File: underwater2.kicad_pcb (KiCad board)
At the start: 2 copper layers, 99.1 x 99.1 mm, 79 parts, among them IC1 ICM-20948, J1 Motor1, J10 ICM20948 out, J11 Pow, J12 serial, J13 serial2, J14 5v pow, J15 5v pow, J2 Motor2, J3 Raspberry_Pi_2_3, J4 USB_C_Receptacle_USB2.0, J5 USB out, J6 Water, J7 Power, J8 Light, J9 MotorPow, SW1 SW_Push, SW2 SW_Push, U1 FT230XS, U2 TB6612FNG, U3 TB6612FNG, U4 ESP32-WROOM-32, U5 LM1117-1.8, U7 LM1117-3.3

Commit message: Modify milestone 2020724
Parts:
- removed PS1: ACT4060ASH-T, SamacSys_Parts:SOIC127P605X175-8N
- removed U7: LM1117-3.3, Package_TO_SOT_SMD:SOT-223
- added C20: 10μF, Capacitor_SMD:C_1206_3216Metric, F.Cu at (168.1, 120.3)
- added IC2: KST10MTF, SOT95P240X120-3N, F.Cu at (155.6, 75.8)
- added IC3: ACT4070BYH-T, SOIC127P600X170-9N, F.Cu at (115.8, 55.6)
- added IC4: ICM-20948, SamacSys_Parts:QFN40P300X300X105-25N-D, F.Cu at (153.7, 63.5)
- added J16: MotorPow, Connector_PinHeader_2.54mm:PinHeader_1x02_P2.54mm_Vertical, F.Cu at (173.2, 120.7)
- added SW3: SW_DIP_x01, Button_Switch_THT:SW_E-Switch_EG1271_DPDT, F.Cu at (123.8, 129.6)
- added U6: TB6612FNG, Package_SO:SSOP-24_5.3x8.2mm_P0.65mm, F.Cu at (161.0, 120.5)
- C1: value 10μF -> 10nF/25V; footprint Capacitor_SMD:C_1206_3216Metric -> Capacitor_SMD:C_0603_1608Metric
- C10: value 10μF -> 1nF/16V; footprint Capacitor_SMD:C_1206_3216Metric -> Capacitor_SMD:C_0603_1608Metric
- C11: value 10nF50V -> 22µF/10V; footprint Capacitor_SMD:C_1206_3216Metric -> Capacitor_SMD:C_0603_1608Metric
- C12, C13: value 0.1μF -> 0μF
- C14: value 22μF10V -> 0.1μF
- C15: value 0.1μF -> 10μF
- C16: value 2.2nF6.3V -> 0.1μF
- C17: value 10μF35V -> 0.1μF
- C18, C19: value 0μF -> 0.1μF
- C2: value 47pF -> 10µF/50V
- C3: value 47pF -> 10nF
- C5: value 0.1μF -> 4.7μF
- C6: value 0.1μF -> 100nF
- C7: value 4.7μF -> 4.7nF/25V; footprint Capacitor_SMD:C_1206_3216Metric -> Capacitor_SMD:C_0603_1608Metric
- C8: value 100nF -> if necessary
- C9: value 10μF -> ifnecessary
- D1: value RX -> 34/40V 3A; footprint Capacitor_SMD:C_1206_3216Metric -> SamacSys_Parts:DIONM7959X282N
- D2: value TX -> 34/40V 3A; footprint Capacitor_SMD:C_1206_3216Metric -> SamacSys_Parts:DIONM7959X282N
- D3: value Power -> TX
- D4: value DIODE -> RX; footprint SamacSys_Parts:DIONM7959X282N -> Capacitor_SMD:C_1206_3216Metric
- D5: value 34/40V 3A -> 40V/3A
- D6: value Power 3.3 -> POWER
- D7: value 34/40V 3A -> Power 3.3; footprint SamacSys_Parts:DIONM7959X282N -> Capacitor_SMD:C_1206_3216Metric
- D8: value 34/40V 3A -> DIODE
- FB1: value FB -> Ferrite_Bead_Small
- IC1: value ICM-20948 -> KST10MTF; footprint SamacSys_Parts:QFN40P300X300X105-25N-D -> SOT95P240X120-3N
- J1: value Motor1 -> 5v pow; footprint Connector_PinSocket_2.54mm:PinSocket_1x04_P2.54mm_Horizontal -> Connector_PinHeader_2.54mm:PinHeader_1x02_P2.54mm_Vertical
- J10: value ICM20948 out -> Power; footprint Connector_PinHeader_2.54mm:PinHeader_1x08_P2.54mm_Vertical -> Connector_PinHeader_2.54mm:PinHeader_1x02_P2.54mm_Horizontal
- J11: value Pow -> Light; footprint Connector_PinHeader_2.54mm:PinHeader_1x02_P2.54mm_Vertical -> Connector_PinHeader_2.54mm:PinHeader_1x03_P2.54mm_Vertical
- J12: value serial -> ICM20948 out; footprint Connector_PinHeader_2.54mm:PinHeader_1x02_P2.54mm_Vertical -> Connector_PinHeader_2.54mm:PinHeader_1x08_P2.54mm_Vertical
- J14: value 5v pow -> Motor1; footprint Connector_PinHeader_2.54mm:PinHeader_1x02_P2.54mm_Vertical -> Connector_PinSocket_2.54mm:PinSocket_1x04_P2.54mm_Horizontal
- J15: value 5v pow -> Motor2; footprint Connector_PinHeader_2.54mm:PinHeader_1x02_P2.54mm_Vertical -> Connector_PinSocket_2.54mm:PinSocket_1x04_P2.54mm_Horizontal
- J2: value Motor2 -> 5v pow; footprint Connector_PinSocket_2.54mm:PinSocket_1x04_P2.54mm_Horizontal -> Connector_PinHeader_2.54mm:PinHeader_1x02_P2.54mm_Vertical
- J3: value Raspberry_Pi_2_3 -> external regurator; footprint Connector_PinSocket_2.54mm:PinSocket_2x20_P2.54mm_Vertical -> Connector_PinSocket_2.54mm:PinSocket_1x03_P2.54mm_Vertical
- J5: value USB out -> Pow; footprint Connector_PinHeader_2.54mm:PinHeader_1x05_P2.54mm_Vertical -> Connector_PinHeader_2.54mm:PinHeader_1x02_P2.54mm_Vertical
- J6: value Water -> Raspberry_Pi_2_3; footprint Connector_PinHeader_2.54mm:PinHeader_1x02_P2.54mm_Horizontal -> Connector_PinSocket_2.54mm:PinSocket_2x20_P2.54mm_Vertical; moved to B.Cu
- J7: value Power -> serial; footprint Connector_PinHeader_2.54mm:PinHeader_1x02_P2.54mm_Horizontal -> Connector_PinHeader_2.54mm:PinHeader_1x02_P2.54mm_Vertical
- J8: value Light -> Conn_01x10_Female; footprint Connector_PinHeader_2.54mm:PinHeader_1x03_P2.54mm_Horizontal -> Connector_PinSocket_2.54mm:PinSocket_1x09_P2.54mm_Vertical
- J9: value MotorPow -> Water; footprint Connector_PinHeader_2.54mm:PinHeader_1x02_P2.54mm_Vertical -> Connector_PinHeader_2.54mm:PinHeader_1x02_P2.54mm_Horizontal
- JP1: value High Full -> Jumper_NC_Small; footprint Jumper:SolderJumper-3_P1.3mm_Open_RoundedPad1.0x1.5mm -> Jumper:SolderJumper-2_P1.3mm_Open_RoundedPad1.0x1.5mm
- JP2: value TX -> J usbpower; footprint Jumper:SolderJumper-2_P1.3mm_Open_Pad1.0x1.5mm -> Jumper:SolderJumper-2_P1.3mm_Open_RoundedPad1.0x1.5mm
- JP3: value RX -> J battpower; footprint Jumper:SolderJumper-2_P1.3mm_Open_Pad1.0x1.5mm -> Jumper:SolderJumper-2_P1.3mm_Open_RoundedPad1.0x1.5mm
- JP4: value J usbpower -> tx rx
- JP5: value J battpower -> rx tx
- L1: value 15μH -> 15µH4A; footprint Capacitor_SMD:C_1206_3216Metric -> SamacSys_Parts:B952ASH100MP3
- R1, R2: value 5.1k -> 10k
- R10: value 10k -> 270
- R11: value 1M -> 51k; footprint Capacitor_SMD:C_1206_3216Metric -> Capacitor_SMD:C_0603_1608Metric
- R12: value 330k -> 9.76k; footprint Capacitor_SMD:C_1206_3216Metric -> Capacitor_SMD:C_0603_1608Metric
- R13: value 28.7k -> 330k
- R14: value 15k -> 12k; footprint Capacitor_SMD:C_1206_3216Metric -> Capacitor_SMD:C_0603_1608Metric
- R15: value 1.5k High -> 270
- R16: value 1.5k Full -> 270
- R3: value 27 -> 10k
- R4: value 27 -> 5.1k
- R5: value 270 -> 5.1k
- R6, R7: value 270 -> 27
- R8: value 10k -> 1M
- SW1, SW2: value SW_Push -> SW_Push_Dual
- U1: value FT230XS -> FT232RL; footprint Package_SO:SSOP-16_3.9x4.9mm_P0.635mm -> Package_SO:SSOP-28_5.3x10.2mm_P0.65mm
- U2: value TB6612FNG -> LM1117-3.3; footprint Package_SO:SSOP-24_5.3x8.2mm_P0.65mm -> Package_TO_SOT_SMD:SOT-223
- U4: value ESP32-WROOM-32 -> LM1117-1.8; footprint RF_Module:ESP32-WROOM-32 -> Package_TO_SOT_SMD:SOT-223
- U5: value LM1117-1.8 -> ESP32-WROOM-32; footprint Package_TO_SOT_SMD:SOT-223 -> RF_Module:ESP32-WROOM-32
- moved R1 91.4 mm to (161.7, 75.9), turned to 180 degrees
- moved J14 90.1 mm to (142.5, 129.0)
- moved J15 88.3 mm to (158.9, 129.2), turned to 90 degrees
- moved J1 86.5 mm to (120.7, 43.9)
- moved R16 85.9 mm to (147.3, 64.4)
- moved J2 85.6 mm to (143.5, 43.8)
- moved C7 84.8 mm to (122.7, 54.1), turned to 0 degrees
- moved JP1 83.5 mm to (159.4, 79.9), turned to 180 degrees
- moved C1 83.0 mm to (110.9, 53.0), turned to 90 degrees
- moved J12 82.8 mm to (169.9, 58.9), turned to 0 degrees
- moved D8 82.5 mm to (170.4, 113.0), turned to 180 degrees
- moved R2 79.9 mm to (151.3, 77.7), turned to 270 degrees
- moved C2 79.7 mm to (108.2, 56.3)
- moved J13 74.6 mm to (103.3, 43.9), turned to 270 degrees
- moved SW2 73.2 mm to (159.0, 53.0), turned to 180 degrees
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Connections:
- C1 pad 2: GND -> Net-(C1-Pad2)
- C10 pad 1: -BATT -> Net-(C10-Pad1)
- C10 pad 2: GND -> Net-(C10-Pad2)
- C11 pad 1: Net-(C11-Pad1) -> Net-(C10-Pad1)
- C11 pad 2: Net-(C11-Pad2) -> GND
- C12 pad 1: Net-(C12-Pad1) -> GND
- C12 pad 2: GND -> Net-(C12-Pad2)
- C13 pad 1: Net-(C13-Pad1) -> GND
- C13 pad 2: GND -> Net-(C13-Pad2)
- C14 pad 1: Net-(C14-Pad1) -> -BATT
- C15 pad 1: +3V3 -> -BATT
- C16 pad 1: Net-(C16-Pad1) -> +3V3
- C16 pad 2: Net-(C16-Pad2) -> GND
- C18 pad 1: GND -> Net-(C18-Pad1)
- C18 pad 2: Net-(C18-Pad2) -> GND
- C19 pad 2: Net-(C19-Pad2) -> -BATT
- C4 pad 1: Net-(C4-Pad1) -> +5V
- C5 pad 1: -BATT -> +5V
- C6 pad 1: GND -> Net-(C6-Pad1)
- C6 pad 2: -BATT -> GND
- C7 pad 1: Net-(C4-Pad1) -> Net-(C7-Pad1)
- C7 pad 2: GND -> Net-(C7-Pad2)
- C9 pad 1: -BATT -> Net-(C9-Pad1)
- D1 pad 1: Net-(D1-Pad1) -> +5V
- D2 pad 2: Net-(D2-Pad2) -> Net-(C2-Pad1)
- D3 pad 1: GND -> Net-(D3-Pad1)
- D3 pad 2: Net-(D3-Pad2) -> Net-(C6-Pad1)
- D4 pad 2: -BATT -> Net-(C6-Pad1)
- D5 pad 1: Net-(C4-Pad1) -> GND
- D5 pad 2: Net-(D5-Pad2) -> Net-(C1-Pad2)
- D6 pad 1: GND -> Net-(D6-Pad1)
- D6 pad 2: Net-(D6-Pad2) -> Net-(C6-Pad1)
- D7 pad 2: Net-(C11-Pad2) -> Net-(D7-Pad2)
- D8 pad 2: Net-(C17-Pad1) -> -BATT
- FB1 pad 1: Net-(C4-Pad1) -> Net-(C3-Pad1)
- FB1 pad 2: Net-(C1-Pad1) -> +5V
- IC1 pad 1: (no net) -> Net-(IC1-Pad1)
- IC1 pad 2: (no net) -> Net-(IC1-Pad2)
- IC1 pad 3: (no net) -> Net-(IC1-Pad3)
- J1 pad 2: Net-(J1-Pad2) -> GND
- J10 pad 1: +3V3 -> Net-(J10-Pad1)
- J11 pad 1: Net-(D8-Pad1) -> Net-(J1-Pad1)
- J11 pad 2: GND -> Net-(J11-Pad2)
- J12 pad 1: Net-(C19-Pad2) -> +3V3
- J12 pad 2: Net-(C18-Pad2) -> GND
- J13 pad 1: Net-(C19-Pad2) -> Net-(C13-Pad2)
- J13 pad 2: Net-(C18-Pad2) -> Net-(C12-Pad2)
- J14 pad 2: GND -> Net-(J14-Pad2)
- J15 pad 1: Net-(J14-Pad1) -> Net-(J15-Pad1)
- J15 pad 2: GND -> Net-(J15-Pad2)
- J2 pad 1: Net-(J2-Pad1) -> Net-(J1-Pad1)
- J2 pad 2: Net-(J2-Pad2) -> GND
- J3 pad 1: (no net) -> Net-(C10-Pad1)
- J3 pad 2: Net-(J14-Pad1) -> GND
- J3 pad 3: (no net) -> Net-(C2-Pad1)
- J4 pad A4: Net-(C1-Pad1) -> Net-(C3-Pad1)
- J4 pad A6: Net-(C2-Pad1) -> Net-(C9-Pad1)
- J4 pad A7: Net-(C3-Pad1) -> Net-(C8-Pad1)
- J4 pad A9: Net-(C1-Pad1) -> Net-(C3-Pad1)
- J4 pad B4: Net-(C1-Pad1) -> Net-(C3-Pad1)
- J4 pad B6: Net-(C3-Pad1) -> Net-(C9-Pad1)
- J4 pad B7: Net-(C2-Pad1) -> Net-(C8-Pad1)
- J4 pad B9: Net-(C1-Pad1) -> Net-(C3-Pad1)
- J5 pad 1: Net-(C4-Pad1) -> Net-(J5-Pad1)
- J5 pad 2: Net-(J5-Pad2) -> GND
- J6 pad 1: Net-(J6-Pad1) -> (no net)
- J6 pad 2: GND -> Net-(J1-Pad1)
- J7 pad 1: Net-(J7-Pad1) -> Net-(C13-Pad2)
- J7 pad 2: GND -> Net-(C12-Pad2)
- J8 pad 1: Net-(J14-Pad1) -> Net-(IC2-Pad2)
- J8 pad 2: Net-(J8-Pad2) -> Net-(IC1-Pad2)
- J8 pad 3: GND -> Net-(J8-Pad3)
- J9 pad 1: Net-(D4-Pad1) -> Net-(J9-Pad1)
- JP1 pad 1: Net-(JP1-Pad1) -> ESP_EN
- JP1 pad 2: Net-(C4-Pad1) -> Net-(IC1-Pad3)
- JP2 pad 1: Net-(J5-Pad2) -> Net-(D1-Pad2)
- JP2 pad 2: Net-(C19-Pad2) -> Net-(J1-Pad1)
- JP3 pad 1: Net-(J5-Pad3) -> Net-(J1-Pad1)
- JP3 pad 2: Net-(C18-Pad2) -> Net-(C10-Pad1)
- JP4 pad 1: Net-(D5-Pad2) -> Net-(JP4-Pad1)
- JP4 pad 2: Net-(J14-Pad1) -> Net-(C12-Pad2)
- JP5 pad 1: Net-(J14-Pad1) -> Net-(JP5-Pad1)
- JP5 pad 2: Net-(C14-Pad1) -> Net-(C13-Pad2)
- JP6 pad 2: Net-(IC1-Pad9) -> Net-(IC4-Pad9)
- JP6 pad 3: Net-(C12-Pad1) -> Net-(C17-Pad1)
- JP7 pad 1: Net-(IC1-Pad11) -> Net-(IC4-Pad11)
- L1 pad 1: Net-(C14-Pad1) -> Net-(C10-Pad1)
- L1 pad 2: Net-(C11-Pad2) -> Net-(C1-Pad2)
- R1 pad 1: GND -> +3V3
- R1 pad 2: Net-(J4-PadA5) -> ESP_EN
- R10 pad 1: Net-(PS1-Pad5) -> Net-(D4-Pad1)
- R10 pad 2: GND -> Net-(R10-Pad2)
- R11 pad 1: Net-(C17-Pad1) -> Net-(C10-Pad1)
- R11 pad 2: Net-(PS1-Pad7) -> Net-(C10-Pad2)
- R12 pad 1: Net-(PS1-Pad7) -> Net-(C10-Pad2)
- R13 pad 1: Net-(C14-Pad1) -> Net-(IC3-Pad7)
- R13 pad 2: Net-(PS1-Pad5) -> GND
- R14 pad 1: Net-(C16-Pad2) -> Net-(C7-Pad2)
- R15 pad 1: Net-(JP1-Pad3) -> Net-(D6-Pad1)
- R15 pad 2: Net-(C3-Pad1) -> GND
- R16 pad 1: Net-(JP1-Pad1) -> +3V3
- R16 pad 2: Net-(C2-Pad1) -> Net-(D7-Pad2)
- R17 pad 1: Net-(C12-Pad1) -> Net-(C17-Pad1)
- R17 pad 2: Net-(IC1-Pad24) -> Net-(IC4-Pad24)
- R18 pad 1: Net-(C12-Pad1) -> Net-(C17-Pad1)
- R18 pad 2: Net-(IC1-Pad23) -> Net-(IC4-Pad23)
- R2 pad 1: GND -> Net-(IC2-Pad2)
- R2 pad 2: Net-(J4-PadB5) -> Net-(IC1-Pad1)
- R3 pad 1: Net-(R3-Pad1) -> Net-(IC1-Pad2)
- R3 pad 2: Net-(C2-Pad1) -> Net-(IC2-Pad1)
- R4 pad 1: Net-(R4-Pad1) -> GND
- R4 pad 2: Net-(C3-Pad1) -> Net-(J4-PadA5)
- R5 pad 1: Net-(C8-Pad1) -> GND
- R5 pad 2: Net-(D1-Pad2) -> Net-(J4-PadB5)
- R6 pad 1: Net-(C8-Pad1) -> Net-(R6-Pad1)
- R6 pad 2: Net-(D2-Pad2) -> Net-(C8-Pad1)
- R7 pad 1: Net-(C8-Pad1) -> Net-(R7-Pad1)
- R7 pad 2: Net-(D3-Pad2) -> Net-(C9-Pad1)
- R8 pad 1: Net-(R8-Pad1) -> Net-(C2-Pad1)
- R8 pad 2: +3V3 -> Net-(IC3-Pad7)
- R9 pad 1: +3V3 -> Net-(D3-Pad1)
- R9 pad 2: Net-(D6-Pad2) -> Net-(R9-Pad2)
- SW1 pad 1: Net-(R8-Pad1) -> GND
- SW1 pad 2: GND -> ESP_EN
- SW2 pad 1: Net-(SW2-Pad1) -> IO0
- U1 pad 1: Net-(J5-Pad2) -> Net-(JP4-Pad1)
- U1 pad 10: Net-(C8-Pad1) -> Net-(J8-Pad5)
- U1 pad 11: Net-(C8-Pad1) -> (no net)
- U1 pad 12: Net-(C4-Pad1) -> (no net)
- U1 pad 13: GND -> (no net)
- U1 pad 14: Net-(D1-Pad1) -> (no net)
- U1 pad 15: (no net) -> Net-(R7-Pad1)
- U1 pad 16: (no net) -> Net-(R6-Pad1)
- U1 pad 2: Net-(J5-Pad4) -> Net-(IC2-Pad2)
- U1 pad 3: Net-(C8-Pad1) -> Net-(IC1-Pad2)
- U1 pad 4: Net-(J5-Pad3) -> +5V
- U1 pad 5: GND -> Net-(JP5-Pad1)
- U1 pad 6: Net-(J5-Pad5) -> Net-(J8-Pad3)
- U1 pad 7: Net-(D2-Pad1) -> GND
- U1 pad 8: Net-(R3-Pad1) -> (no net)
- U1 pad 9: Net-(R4-Pad1) -> Net-(J8-Pad4)
- U2 pad 1: Net-(J1-Pad1) -> GND
- U2 pad 2: Net-(J1-Pad1) -> +3V3
- U2 pad 3: GND -> Net-(J1-Pad1)
- U2 pad 4: GND -> (no net)
- U3 pad 1: Net-(J2-Pad1) -> Net-(J14-Pad1)
- U3 pad 11: Net-(J2-Pad3) -> Net-(J14-Pad3)
- U3 pad 12: Net-(J2-Pad3) -> Net-(J14-Pad3)
- U3 pad 2: Net-(J2-Pad1) -> Net-(J14-Pad1)
- U3 pad 5: Net-(J2-Pad2) -> Net-(J14-Pad2)
- U3 pad 6: Net-(J2-Pad2) -> Net-(J14-Pad2)
- U3 pad 7: Net-(J2-Pad4) -> Net-(J14-Pad4)
- U3 pad 8: Net-(J2-Pad4) -> Net-(J14-Pad4)
- U4 pad 2: +3V3 -> Net-(C17-Pad1)
- U4 pad 3: Net-(R8-Pad1) -> +3V3
- U5 pad 2: Net-(C12-Pad1) -> +3V3
- U5 pad 3: +3V3 -> ESP_EN
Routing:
- net Net-(J1-Pad1): track 10.0 -> 206.4 mm, vias 0 -> 2
- net Net-(C13-Pad2): track 0.00 -> 195.2 mm, vias 0 -> 7
- net Net-(C19-Pad2): track 190.6 -> 0.00 mm, vias 4 -> 0
- net Net-(J14-Pad1): track 200.2 -> 10.9 mm, vias 3 -> 0
- net Net-(C12-Pad2): track 0.00 -> 184.0 mm, vias 0 -> 5
- net Net-(C18-Pad2): track 184.0 -> 0.00 mm, vias 4 -> 0
- net +5V: track 0.00 -> 99.2 mm, vias 0 -> 3
- net Net-(C4-Pad1): track 98.2 -> 0.00 mm, vias 10 -> 0
- net Net-(IC1-Pad23): track 89.7 -> 0.00 mm, vias 4 -> 0
- net Net-(IC4-Pad24): track 0.00 -> 82.9 mm, vias 0 -> 8
- net Net-(IC1-Pad24): track 82.8 -> 0.00 mm, vias 6 -> 0
- net Net-(IC2-Pad2): track 0.00 -> 82.3 mm, vias 0 -> 6
- net Net-(IC1-Pad2): track 0.00 -> 81.4 mm, vias 0 -> 4
- net Net-(C6-Pad1): track 0.00 -> 80.3 mm, vias 0 -> 1
- net IO0: track 0.00 -> 77.5 mm, vias 0 -> 4
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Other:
- board size 99.1 x 99.1 mm -> 83.8 x 99.1 mm

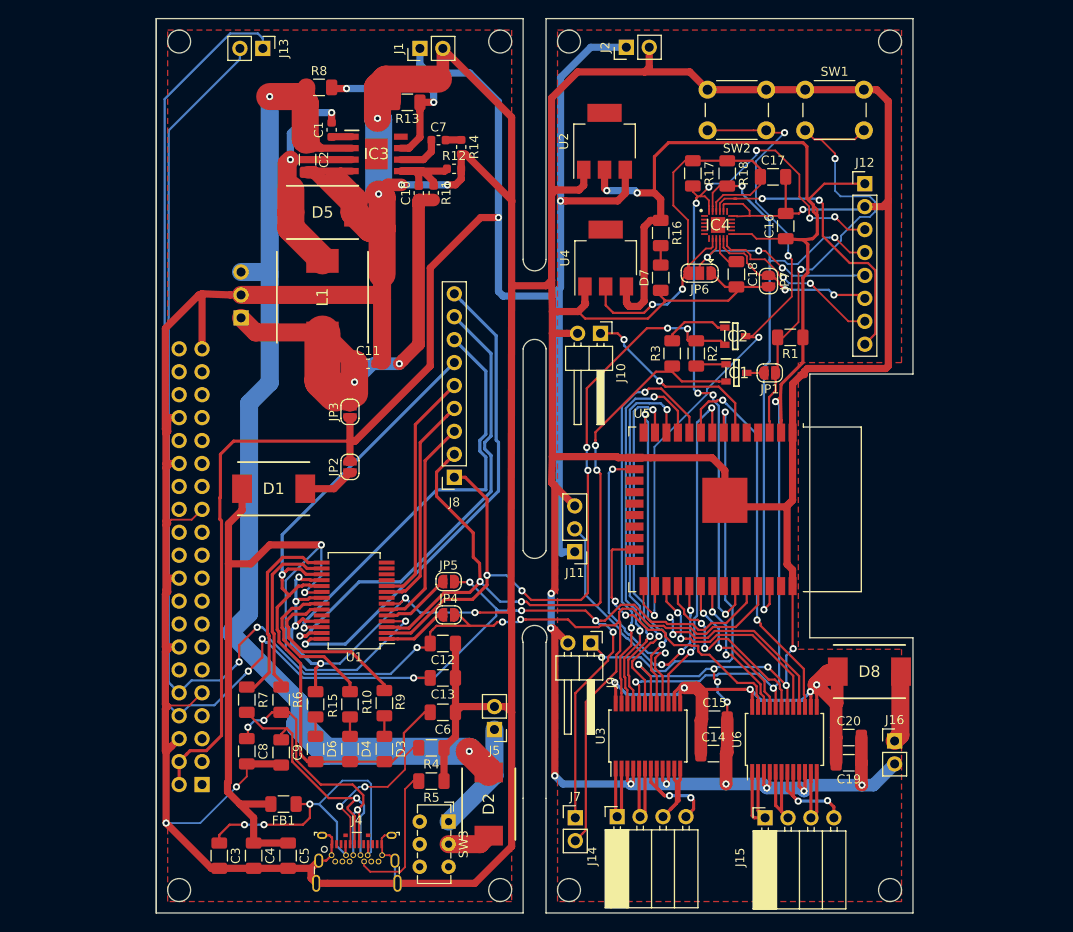
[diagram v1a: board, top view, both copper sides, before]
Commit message: Add broken charger.
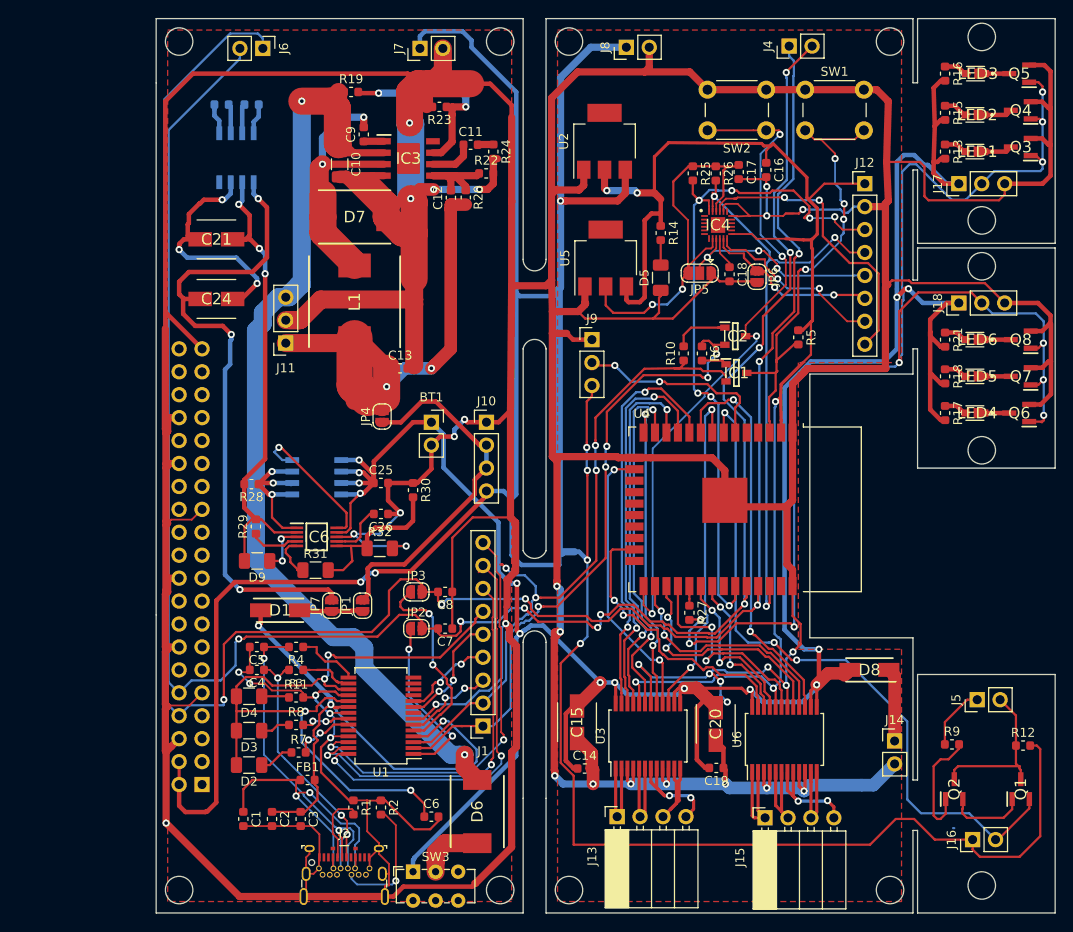
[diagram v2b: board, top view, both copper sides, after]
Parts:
- removed the J3 at (100.8, 73.8)
- removed the J5 at (128.9, 119.4)
- removed the JP1 at (159.4, 79.9)
- added BT1: Battery, Connector_PinSocket_2.54mm:PinSocket_1x02_P2.54mm_Vertical, F.Cu at (121.9, 85.3)
- added C21: 10μF, SamacSys_Parts:865080640004, F.Cu at (98.1, 65.1)
- added C22: 0.22μF, Capacitor_SMD:C_0603_1608Metric, B.Cu at (98.7, 50.2)
- added C23: 0.22μF, Capacitor_SMD:C_0603_1608Metric, B.Cu at (102.0, 50.2)
- added C24: 4.7uF, SamacSys_Parts:865080640004, F.Cu at (98.1, 71.7)
- added C25: 10μF, Capacitor_SMD:C_0603_1608Metric, F.Cu at (116.3, 92.1)
- added C26: 0.1μF, Capacitor_SMD:C_0603_1608Metric, F.Cu at (116.3, 95.5)
- added D9: LED_Small, Capacitor_SMD:C_1206_3216Metric, F.Cu at (102.6, 100.7)
- added IC5: MAX662ACSA+, SamacSys_Parts:SOIC127P600X175-8N, B.Cu at (100.3, 56.1)
- added IC6: MCP73842T-840I_UN, SamacSys_Parts:SOP50P490X110-10N, F.Cu at (109.2, 98.0)
- added J10: momentary switch, Connector_PinHeader_2.54mm:PinHeader_1x04_P2.54mm_Vertical, F.Cu at (128.0, 85.3)
- added J16: Conn_01x02_Female, Connector_PinHeader_2.54mm:PinHeader_1x02_P2.54mm_Vertical, F.Cu at (181.9, 131.6)
- added J17: Conn_01x02_Female, Connector_PinHeader_2.54mm:PinHeader_1x03_P2.54mm_Vertical, F.Cu at (180.3, 58.9)
- added J18: Conn_01x02_Female, Connector_PinHeader_2.54mm:PinHeader_1x03_P2.54mm_Vertical, F.Cu at (180.3, 72.1)
- added JP7: charge, Jumper:SolderJumper-2_P1.3mm_Open_RoundedPad1.0x1.5mm, F.Cu at (110.9, 105.7)
- added LED1: MP-2016-1100-65-70, SamacSys_Parts:MP201611006570, F.Cu at (182.1, 55.4)
- added LED2: MP-2016-1100-65-70, SamacSys_Parts:MP201611006570, F.Cu at (182.1, 51.3)
- added LED3: MP-2016-1100-65-70, SamacSys_Parts:MP201611006570, F.Cu at (182.2, 46.7)
- added LED4: MP-2016-1100-65-70, SamacSys_Parts:MP201611006570, F.Cu at (182.1, 84.3)
- added LED5: MP-2016-1100-65-70, SamacSys_Parts:MP201611006570, F.Cu at (182.1, 80.3)
- added LED6: MP-2016-1100-65-70, SamacSys_Parts:MP201611006570, F.Cu at (182.1, 76.2)
- added Q1: 2SC2712-Y,LF, SamacSys_Parts:SOT95P260X140-3N, F.Cu at (187.2, 126.0)
- added Q2: 2SC2712-Y,LF, SamacSys_Parts:SOT95P260X140-3N, F.Cu at (179.8, 126.0)
- added Q3: 2SC2712-Y,LF, SamacSys_Parts:SOT95P260X140-3N, F.Cu at (187.2, 54.9)
- added Q4: 2SC2712-Y,LF, SamacSys_Parts:SOT95P260X140-3N, F.Cu at (187.2, 50.8)
- added Q5: 2SC2712-Y,LF, SamacSys_Parts:SOT95P260X140-3N, F.Cu at (187.0, 46.7)
- added Q6: 2SC2712-Y,LF, SamacSys_Parts:SOT95P260X140-3N, F.Cu at (187.0, 84.3)
- added Q7: 2SC2712-Y,LF, SamacSys_Parts:SOT95P260X140-3N, F.Cu at (187.2, 80.3)
- added Q8: 2SC2712-Y,LF, SamacSys_Parts:SOT95P260X140-3N, F.Cu at (187.2, 76.2)
- added Q9: NDS8434, SamacSys_Parts:SOIC127P600X175-8N, B.Cu at (109.2, 91.4)
- added R12: 1k, Capacitor_SMD:C_0603_1608Metric, F.Cu at (187.5, 121.2)
- added R13: 67, Capacitor_SMD:C_0603_1608Metric, F.Cu at (178.8, 55.4)
- added R15: 67, Capacitor_SMD:C_0603_1608Metric, F.Cu at (178.8, 51.1)
- added R16: 67, Capacitor_SMD:C_0603_1608Metric, F.Cu at (178.8, 46.7)
- added R17: 67, Capacitor_SMD:C_0603_1608Metric, F.Cu at (178.8, 84.3)
- added R18: 67, Capacitor_SMD:C_0603_1608Metric, F.Cu at (178.8, 80.3)
- added R21: 67, Capacitor_SMD:C_0603_1608Metric, F.Cu at (178.8, 76.2)
- added R27: 100, Capacitor_SMD:C_0603_1608Metric, F.Cu at (150.5, 106.5)
- added R28: 100m, Capacitor_SMD:C_0603_1608Metric, F.Cu at (102.0, 92.2)
- added R29: 100k, Capacitor_SMD:C_0603_1608Metric, F.Cu at (102.5, 96.9)
- added R30: R_Variable, Capacitor_SMD:C_0603_1608Metric, F.Cu at (119.9, 92.9)
- added R31: sermal1, Capacitor_SMD:C_1206_3216Metric, F.Cu at (109.1, 101.7)
- added R32: sermal2, Capacitor_SMD:C_1206_3216Metric, F.Cu at (116.2, 99.3)
- added R9: 1k, Capacitor_SMD:C_0603_1608Metric, F.Cu at (179.6, 121.0)
- C1: renamed from C3; footprint Capacitor_SMD:C_1206_3216Metric -> Capacitor_SMD:C_0603_1608Metric
- C14, C16, C17, C18, C19, C6, FB1: footprint Capacitor_SMD:C_1206_3216Metric -> Capacitor_SMD:C_0603_1608Metric
- C15, C20: footprint Capacitor_SMD:C_1206_3216Metric -> SamacSys_Parts:865080640004
- C2: renamed from C4; footprint Capacitor_SMD:C_1206_3216Metric -> Capacitor_SMD:C_0603_1608Metric
- C3: renamed from C5; footprint Capacitor_SMD:C_1206_3216Metric -> Capacitor_SMD:C_0603_1608Metric
- C4: renamed from C8; footprint Capacitor_SMD:C_1206_3216Metric -> Capacitor_SMD:C_0603_1608Metric
- C5: renamed from C9; value ifnecessary -> if necessary; footprint Capacitor_SMD:C_1206_3216Metric -> Capacitor_SMD:C_0603_1608Metric
- C7: renamed from C12; footprint Capacitor_SMD:C_1206_3216Metric -> Capacitor_SMD:C_0603_1608Metric
- C8: renamed from C13; footprint Capacitor_SMD:C_1206_3216Metric -> Capacitor_SMD:C_0603_1608Metric
- D1, D8: footprint SamacSys_Parts:DIONM7959X282N -> SamacSys_Parts:DIOM5226X240N
- IC1, IC2: footprint SOT95P240X120-3N -> SamacSys_Parts:SOT95P240X120-3N
- IC3: footprint SOIC127P600X170-9N -> SamacSys_Parts:SOIC127P600X170-9N
- J11: value Light -> external regurator; footprint Connector_PinHeader_2.54mm:PinHeader_1x03_P2.54mm_Vertical -> Connector_PinSocket_2.54mm:PinSocket_1x03_P2.54mm_Vertical
- J5: renamed from J9; footprint Connector_PinHeader_2.54mm:PinHeader_1x02_P2.54mm_Horizontal -> Connector_PinHeader_2.54mm:PinHeader_1x02_P2.54mm_Vertical
- J9: renamed from J10; footprint Connector_PinHeader_2.54mm:PinHeader_1x02_P2.54mm_Horizontal -> Connector_PinHeader_2.54mm:PinHeader_1x03_P2.54mm_Vertical
- R1: renamed from R4; footprint Capacitor_SMD:C_1206_3216Metric -> Capacitor_SMD:C_0603_1608Metric
- R10: renamed from R3; footprint Capacitor_SMD:C_1206_3216Metric -> Capacitor_SMD:C_0603_1608Metric
- R11: renamed from R15; footprint Capacitor_SMD:C_1206_3216Metric -> Capacitor_SMD:C_0603_1608Metric
- R14: renamed from R16; footprint Capacitor_SMD:C_1206_3216Metric -> Capacitor_SMD:C_0603_1608Metric
- R19: renamed from R8; footprint Capacitor_SMD:C_1206_3216Metric -> Capacitor_SMD:C_0603_1608Metric
- R2: renamed from R5; footprint Capacitor_SMD:C_1206_3216Metric -> Capacitor_SMD:C_0603_1608Metric
- R23: renamed from R13; footprint Capacitor_SMD:C_1206_3216Metric -> Capacitor_SMD:C_0603_1608Metric
- R25: renamed from R17; footprint Capacitor_SMD:C_1206_3216Metric -> Capacitor_SMD:C_0603_1608Metric
- R26: renamed from R18; footprint Capacitor_SMD:C_1206_3216Metric -> Capacitor_SMD:C_0603_1608Metric
- R3: renamed from R6; footprint Capacitor_SMD:C_1206_3216Metric -> Capacitor_SMD:C_0603_1608Metric
- R4: renamed from R7; footprint Capacitor_SMD:C_1206_3216Metric -> Capacitor_SMD:C_0603_1608Metric
- R5: renamed from R1; footprint Capacitor_SMD:C_1206_3216Metric -> Capacitor_SMD:C_0603_1608Metric
- R6: renamed from R2; footprint Capacitor_SMD:C_1206_3216Metric -> Capacitor_SMD:C_0603_1608Metric
- R7: renamed from R9; footprint Capacitor_SMD:C_1206_3216Metric -> Capacitor_SMD:C_0603_1608Metric
- R8: renamed from R10; footprint Capacitor_SMD:C_1206_3216Metric -> Capacitor_SMD:C_0603_1608Metric
- moved J4 88.7 mm to (161.5, 43.7), turned to 90 degrees
- moved J5 43.3 mm to (182.4, 116.1), turned to 90 degrees
- moved J11 39.5 mm to (105.8, 76.6)
- moved J1 27.7 mm to (127.6, 119.0)
- moved JP1 15.4 mm to (114.3, 105.7)
- moved C15 15.2 mm to (138.0, 118.6), turned to 90 degrees
- moved D2 15.1 mm to (101.7, 123.3), turned to 180 degrees
- moved C20 14.8 mm to (153.4, 118.8), turned to 90 degrees
- moved C19 14.7 mm to (153.5, 123.6)
- moved C14 14.4 mm to (138.9, 123.7)
- moved D1 13.5 mm to (105.2, 106.2)
- moved U1 13.1 mm to (116.3, 117.9)
- moved C5 12.0 mm to (102.6, 110.2), turned to 180 degrees
- moved C6 11.6 mm to (121.9, 129.0)
- moved D3 11.4 mm to (101.7, 119.5), turned to 180 degrees
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- renumbered C2 to C10, C7 to C11, C10 to C12, C11 to C13, C1 to C9, D3 to D2, D4 to D3, D6 to D4, D7 to D5, D2 to D6, D5 to D7, J8 to J1, J14 to J13, J16 to J14, J4 to J2, J6 to J3, J7 to J4, J13 to J6, J1 to J7, J2 to J8, JP2 to JP1, JP4 to JP2, JP5 to JP3, JP3 to JP4, JP6 to JP5, JP7 to JP6, R11 to R20, R12 to R22, R14 to R24, U5 to U4, U4 to U5
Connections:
- net Net-(C6-Pad1) renamed USB_NRESET
- net Net-(IC1-Pad2) renamed USB_RTS
- net Net-(IC2-Pad2) renamed USB_DTR
- net Net-(IC4-Pad23) renamed SCL
- net Net-(IC4-Pad24) renamed SDA
- net Net-(J8-Pad3) renamed USB_RI
- net Net-(JP4-Pad1) renamed USB_TXD
- net Net-(JP5-Pad1) renamed USB_RXD
- net Net-(R6-Pad1) renamed USBD-
- net Net-(R7-Pad1) renamed USBD+
- net Net-(U3-Pad15) renamed IO32
- net Net-(U3-Pad16) renamed IO13
- net Net-(U3-Pad17) renamed IO12
- net Net-(U3-Pad19) renamed IO14
- net Net-(U3-Pad21) renamed IO27
- net Net-(U3-Pad22) renamed IO26
- net Net-(U3-Pad23) renamed IO25
- net Net-(U5-Pad23) renamed IO15
- net Net-(U5-Pad26) renamed IO4
- net Net-(U5-Pad27) renamed IO16
- net Net-(U5-Pad28) renamed IO17
- net Net-(U5-Pad30) renamed IO18
- net Net-(U5-Pad31) renamed IO19
- net Net-(U5-Pad9) renamed IO33
- C1 pad 2: GND -> -BATT
- C10 pad 1: Net-(C2-Pad1) -> Net-(C10-Pad1)
- C10 pad 2: GND -> -BATT
- C12 pad 1: Net-(C10-Pad1) -> Net-(C12-Pad1)
- C13 pad 1: Net-(C10-Pad1) -> Net-(C12-Pad1)
- C13 pad 2: GND -> -BATT
- C14 pad 1: -BATT -> +BATT
- C14 pad 2: GND -> -BATT
- C15 pad 1: -BATT -> +BATT
- C15 pad 2: GND -> -BATT
- C16 pad 2: GND -> -BATT
- C17 pad 2: GND -> -BATT
- C18 pad 2: GND -> -BATT
- C19 pad 1: GND -> -BATT
- C19 pad 2: -BATT -> +BATT
- C2 pad 1: +5V -> Net-(C2-Pad1)
- C2 pad 2: GND -> -BATT
- C20 pad 1: -BATT -> +BATT
- C20 pad 2: GND -> -BATT
- C3 pad 1: +5V -> Net-(C2-Pad1)
- C3 pad 2: GND -> -BATT
- C4 pad 2: GND -> -BATT
- C5 pad 2: GND -> -BATT
- C6 pad 2: GND -> -BATT
- C7 pad 1: GND -> -BATT
- C7 pad 2: Net-(C12-Pad2) (its old number) -> RXD0
- C8 pad 1: GND -> -BATT
- C8 pad 2: Net-(C13-Pad2) -> TXD0
- D1 pad 1: +5V -> Net-(C2-Pad1)
- D5 pad 1: GND -> -BATT
- D6 pad 2: Net-(C2-Pad1) -> Net-(C10-Pad1)
- D7 pad 1: GND -> -BATT
- D8 pad 2: -BATT -> +BATT
- FB1 pad 2: +5V -> Net-(C2-Pad1)
- IC1 pad 3: Net-(IC1-Pad3) -> ESP_EN
- IC3 pad 2: Net-(C2-Pad1) -> Net-(C10-Pad1)
- IC3 pad 4: GND -> -BATT
- IC4 pad 18: GND -> -BATT
- IC4 pad 20: GND -> -BATT
- J1 pad 4: Net-(J8-Pad4) -> USB_DCD
- J1 pad 5: Net-(J8-Pad5) -> USB_DCR
- J1 pad 7: Net-(J8-Pad7) -> USB_OSCI
- J1 pad 8: Net-(J8-Pad8) -> USB_OSCO
- J1 pad 9: Net-(J8-Pad9) -> USB_TEST
- J11 pad 1: Net-(J1-Pad1) -> Net-(C12-Pad1)
- J11 pad 2: Net-(J11-Pad2) -> -BATT
- J11 pad 3: GND -> Net-(C10-Pad1)
- J12 pad 2: GND -> -BATT
- J14 pad 2: GND -> -BATT
- J2 pad A1: GND -> -BATT
- J2 pad A12: GND -> -BATT
- J2 pad B1: GND -> -BATT
- J2 pad B12: GND -> -BATT
- J2 pad SH: GND -> -BATT
- J3 pad 10: Net-(C12-Pad2) (its old number) -> RXD0
- J3 pad 14: GND -> -BATT
- J3 pad 2: Net-(J1-Pad1) -> +5V
- J3 pad 20: GND -> -BATT
- J3 pad 25: GND -> -BATT
- J3 pad 30: GND -> -BATT
- J3 pad 34: GND -> -BATT
- J3 pad 39: GND -> -BATT
- J3 pad 4: Net-(J1-Pad1) -> +5V
- J3 pad 6: GND -> -BATT
- J3 pad 8: Net-(C13-Pad2) -> TXD0
- J3 pad 9: GND -> -BATT
- J4 pad 1: Net-(C13-Pad2) -> TXD0
- J4 pad 2: Net-(C12-Pad2) (its old number) -> RXD0
- J5 pad 1: Net-(J9-Pad1) -> Net-(J5-Pad1)
- J5 pad 2: GND -> Net-(J5-Pad2)
- J6 pad 1: Net-(C13-Pad2) -> TXD0
- J6 pad 2: Net-(C12-Pad2) (its old number) -> RXD0
- J7 pad 1: Net-(J1-Pad1) -> +5V
- J7 pad 2: GND -> -BATT
- J8 pad 1: Net-(J1-Pad1) -> +5V
- J8 pad 2: GND -> -BATT
- J9 pad 1: Net-(J10-Pad1) -> -BATT
- J9 pad 2: GND -> power
- JP1 pad 2: Net-(J1-Pad1) -> +VSW
- JP2 pad 2: Net-(C12-Pad2) (its old number) -> RXD0
- JP3 pad 2: Net-(C13-Pad2) -> TXD0
- JP4 pad 1: Net-(J1-Pad1) -> +VSW
- JP4 pad 2: Net-(C10-Pad1) -> Net-(C12-Pad1)
- JP5 pad 1: GND -> -BATT
- JP6 pad 2: GND -> -BATT
- L1 pad 1: Net-(C10-Pad1) -> Net-(C12-Pad1)
- R1 pad 1: GND -> -BATT
- R11 pad 2: GND -> -BATT
- R19 pad 1: Net-(C2-Pad1) -> Net-(C10-Pad1)
- R2 pad 1: GND -> -BATT
- R20 pad 1: Net-(C10-Pad1) -> Net-(C12-Pad1)
- R22 pad 2: GND -> -BATT
- R23 pad 2: GND -> -BATT
- R24 pad 2: GND -> -BATT
- SW1 pad 1: GND -> -BATT
- SW2 pad 2: GND -> -BATT
- SW3 pad 1: Net-(J5-Pad1) -> +BATT
- U1 pad 10: Net-(J8-Pad5) -> USB_DCD
- U1 pad 18: GND -> -BATT
- U1 pad 20: +5V -> Net-(C2-Pad1)
- U1 pad 21: GND -> -BATT
- U1 pad 25: GND -> -BATT
- U1 pad 26: Net-(J8-Pad7) -> USB_TEST
- U1 pad 27: Net-(J8-Pad8) -> USB_OSCI
- U1 pad 28: Net-(J8-Pad9) -> USB_OSCO
- U1 pad 4: +5V -> Net-(C2-Pad1)
- U1 pad 7: GND -> -BATT
- U1 pad 9: Net-(J8-Pad4) -> USB_DCR
- U2 pad 1: GND -> -BATT
- U2 pad 3: Net-(J1-Pad1) -> +5V
- U3 pad 10: GND -> -BATT
- U3 pad 13: -BATT -> +BATT
- U3 pad 14: -BATT -> +BATT
- U3 pad 18: GND -> -BATT
- U3 pad 24: -BATT -> +BATT
- U3 pad 3: GND -> -BATT
- U3 pad 4: GND -> -BATT
- U3 pad 9: GND -> -BATT
- U4 pad 1: GND -> -BATT
- U4 pad 15: GND -> -BATT
- U4 pad 29: Net-(J11-Pad2) -> Net-(R27-Pad1)
- U4 pad 34: Net-(C13-Pad2) -> RXD0
- U4 pad 35: Net-(C12-Pad2) (its old number) -> TXD0
- U4 pad 38: GND -> -BATT
- U4 pad 39: GND -> -BATT
- U4 pad 6: Net-(J10-Pad1) -> power
- U4 pad 7: Net-(J9-Pad1) -> WATER
- U5 pad 1: GND -> -BATT
- U6 pad 10: GND -> -BATT
- U6 pad 13: -BATT -> +BATT
- U6 pad 14: -BATT -> +BATT
- U6 pad 18: GND -> -BATT
- U6 pad 24: -BATT -> +BATT
- U6 pad 3: GND -> -BATT
- U6 pad 4: GND -> -BATT
- U6 pad 9: GND -> -BATT
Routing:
- net -BATT: track 62.2 -> 1037.0 mm, vias 5 -> 39
- net GND: track 838.2 -> 0.00 mm, vias 29 -> 0
- net +BATT: track 0.00 -> 302.1 mm, vias 0 -> 14
- net +5V: track 99.2 -> 345.4 mm, vias 3 -> 7
- net TXD0: track 0.00 -> 235.0 mm, vias 0 -> 6
- net RXD0: track 0.00 -> 222.7 mm, vias 0 -> 9
- net Net-(J1-Pad1): track 206.4 -> 0.00 mm, vias 2 -> 0
- net Net-(C13-Pad2): track 195.2 -> 0.00 mm, vias 7 -> 0
- net Net-(C12-Pad2) (its old number): track 184.0 -> 0.00 mm, vias 5 -> 0
- net LED_SW: track 0.00 -> 150.7 mm, vias 0 -> 10
- net WATER: track 0.00 -> 76.5 mm, vias 0 -> 3
- net VCC: track 0.00 -> 72.0 mm, vias 0 -> 3
- net Net-(C12-Pad1): track 0.00 -> 57.0 mm, vias 0 -> 2
- net Net-(C2-Pad1): track 118.9 -> 64.2 mm, vias 2 -> 3
- net Net-(J8-Pad9): track 54.4 -> 0.00 mm, vias 1 -> 0
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- added copper zone on F.Cu, net -BATT
- removed copper zone on F.Cu, net GND
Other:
- board size 83.8 x 99.1 mm -> 99.6 x 99.1 mm
